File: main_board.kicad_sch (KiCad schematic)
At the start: 15 parts, among them J1 MEGA_SARJ, J2 POWER, J3 I2C, J4 FREE_GPIO, J5 5V, J6 12V, J7 24V, J8 GND, J9 GND, U1 BNO055_IMU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

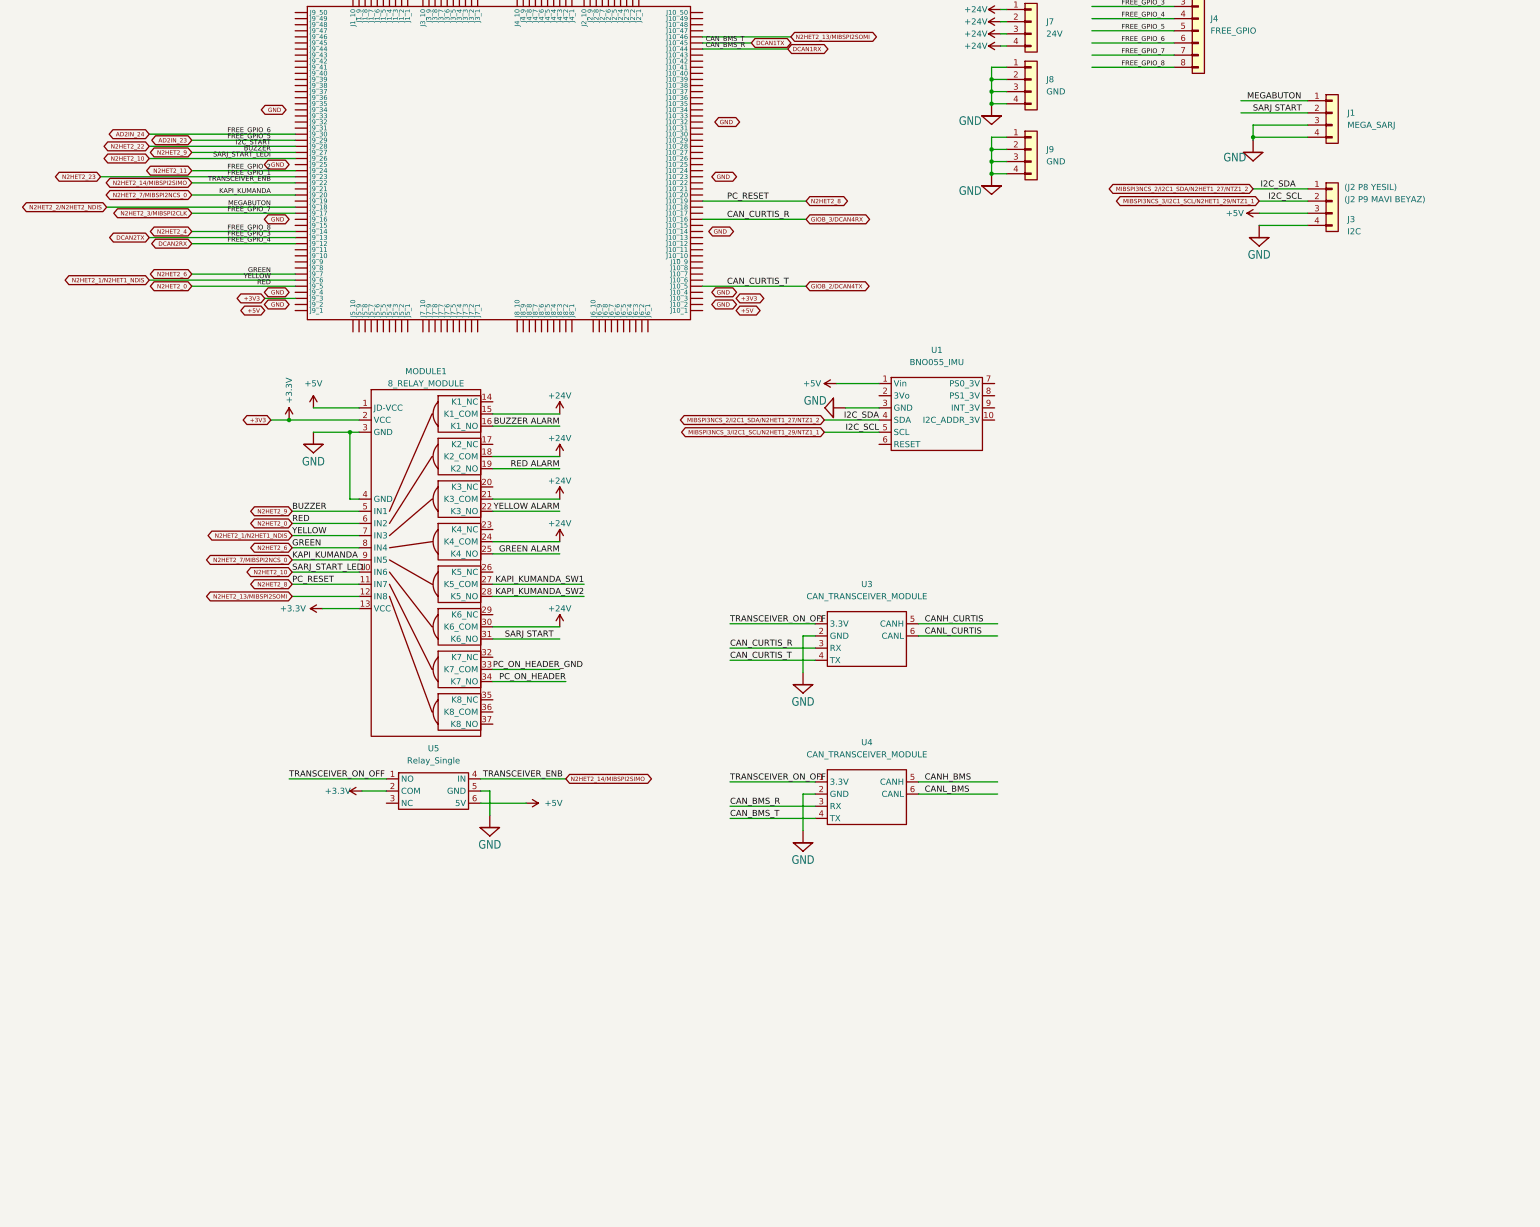
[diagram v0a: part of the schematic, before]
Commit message: Deleting Relays Adding MOSFETs
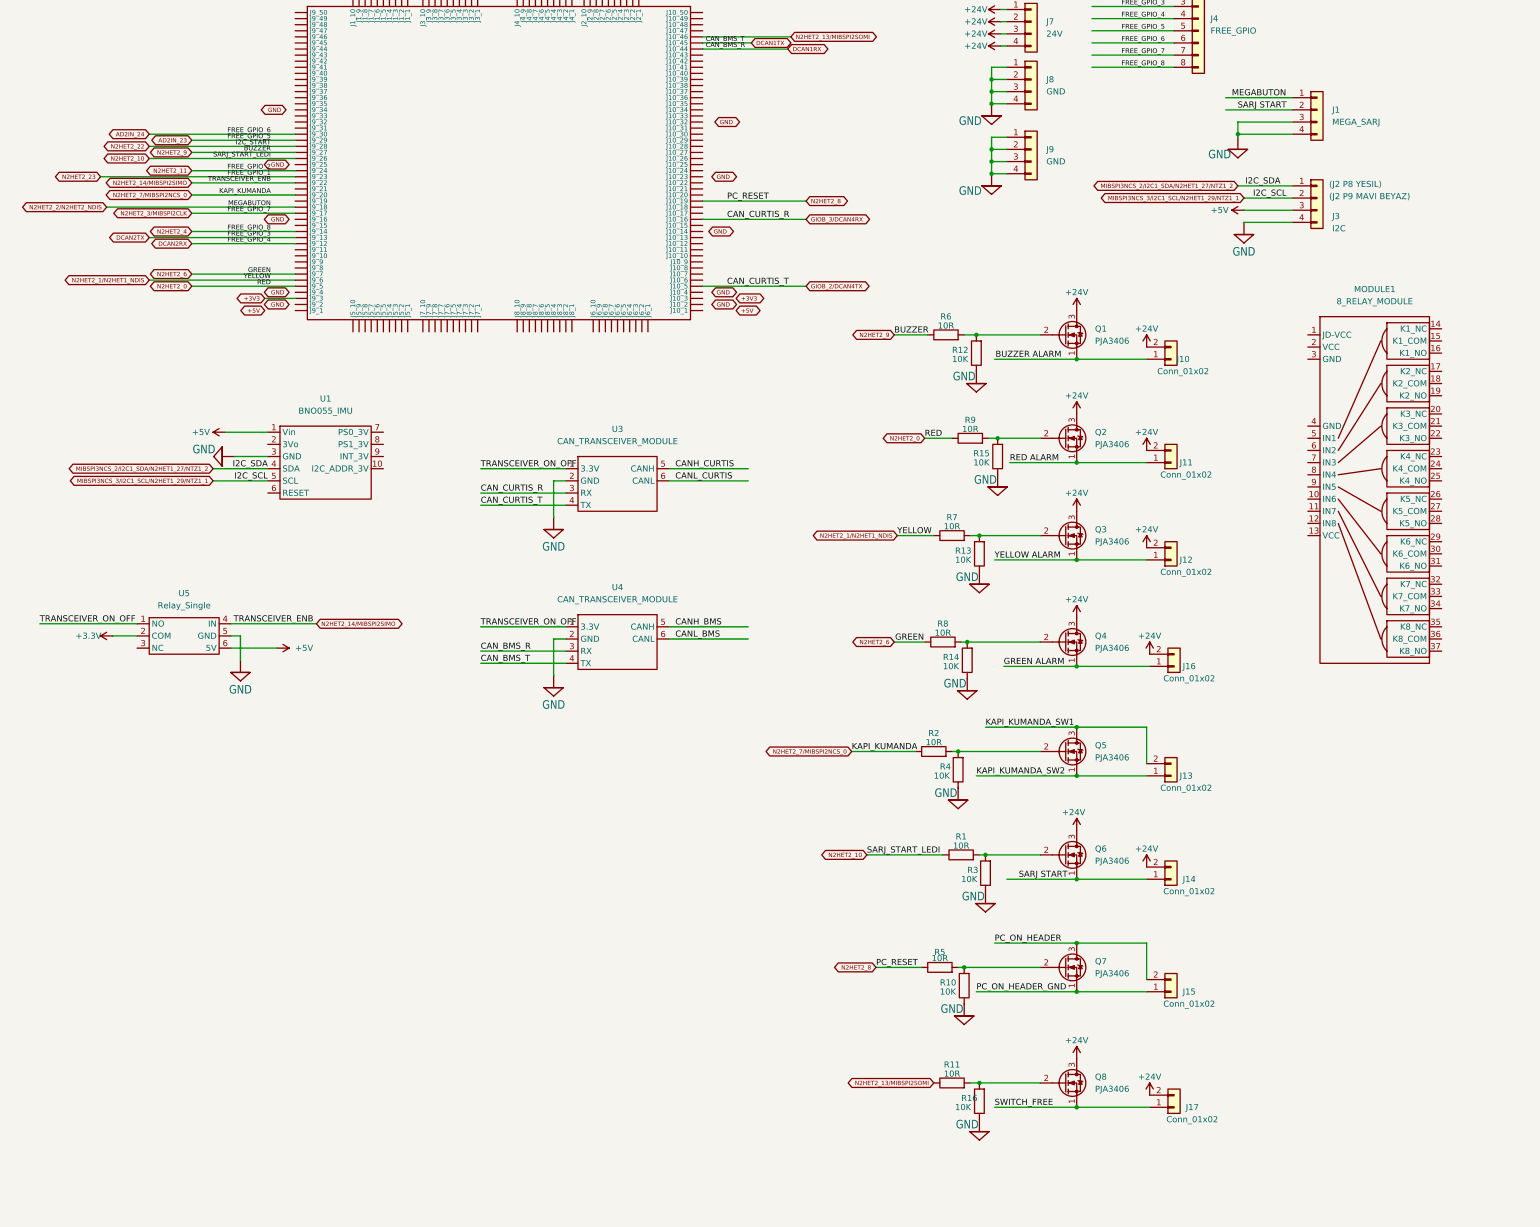
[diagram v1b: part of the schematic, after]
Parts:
- added J10, J11, J12, J13, J14, J15, J16, J17: Conn_01x02, Connector_Phoenix_MC_HighVoltage:PhoenixContact_MCV_1,5_2-G-5.08_1x02_P5.08mm_Vertical, symbol Connector_Generic:Conn_01x02
- added Q1, Q2, Q3, Q4, Q5, Q6, Q7, Q8: PJA3406, Package_TO_SOT_SMD:SOT-23, symbol Transistor_FET:2N7000
- added R1, R11, R2, R5, R6, R7, R8, R9: 10R, Resistor_SMD:R_0805_2012Metric, symbol Device:R
- added R10, R12, R13, R14, R15, R16, R3, R4: 10K, Resistor_SMD:R_0805_2012Metric, symbol Device:R
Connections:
- net +24V: now also J10.2 (Pin_2), J11.2 (Pin_2), J12.2 (Pin_2), J14.2 (Pin_2), J16.2 (Pin_2), J17.2 (Pin_2), Q1.3 (D), Q2.3 (D), Q3.3 (D), Q4.3 (D), Q6.3 (D), Q8.3 (D); no longer MODULE1.15 (K1_COM), MODULE1.18 (K2_COM), MODULE1.21 (K3_COM), MODULE1.24 (K4_COM), MODULE1.30 (K6_COM)
- net +3.3V: no longer MODULE1.13 (VCC), MODULE1.2 (VCC), U2.J9_3
- net +5V: no longer MODULE1.1 (JD-VCC)
- net BUZZER ALARM: now also J10.1 (Pin_1), Q1.1 (S); no longer MODULE1.16 (K1_NO)
- net GND: now also R10.1, R12.1, R13.1, R14.1, R15.1, R16.1, R3.1, R4.1; no longer MODULE1.3 (GND), MODULE1.4 (GND)
- net GREEN ALARM: now also J16.1 (Pin_1), Q4.1 (S); no longer MODULE1.25 (K4_NO)
- net KAPI_KUMANDA_SW1: now also J13.2 (Pin_2), Q5.3 (D); no longer MODULE1.27 (K5_COM)
- net KAPI_KUMANDA_SW2: now also J13.1 (Pin_1), Q5.1 (S); no longer MODULE1.28 (K5_NO)
- net N2HET2_0: now also R9.1; no longer MODULE1.6 (IN2)
- net N2HET2_1/N2HET1_NDIS: now also R7.1; no longer MODULE1.7 (IN3)
- net N2HET2_10: now also R1.1; no longer MODULE1.10 (IN6)
- net N2HET2_13/MIBSPI2SOMI: now also R11.1; no longer MODULE1.12 (IN8)
- net N2HET2_6: now also R8.1; no longer MODULE1.8 (IN4)
- net N2HET2_7/MIBSPI2NCS_0: now also R2.1; no longer MODULE1.9 (IN5)
- net N2HET2_8: now also R5.1; no longer MODULE1.11 (IN7)
- net N2HET2_9: now also R6.1; no longer MODULE1.5 (IN1)
- net PC_ON_HEADER: now also J15.2 (Pin_2), Q7.3 (D); no longer MODULE1.34 (K7_NO)
- net PC_ON_HEADER_GND: now also J15.1 (Pin_1), Q7.1 (S); no longer MODULE1.33 (K7_COM)
- net RED ALARM: now also J11.1 (Pin_1), Q2.1 (S); no longer MODULE1.19 (K2_NO)
- net SARJ START: now also J14.1 (Pin_1), Q6.1 (S); no longer MODULE1.31 (K6_NO)
- net YELLOW ALARM: now also J12.1 (Pin_1), Q3.1 (S); no longer MODULE1.22 (K3_NO)
- new net: Q8.2 (G), R11.2, R16.2
- new net: Q7.2 (G), R10.2, R5.2
- new net: Q2.2 (G), R15.2, R9.2
- new net: Q5.2 (G), R2.2, R4.2
- new net: Q6.2 (G), R1.2, R3.2
- new net: Q1.2 (G), R12.2, R6.2
- new net: Q3.2 (G), R13.2, R7.2
- new net: Q4.2 (G), R14.2, R8.2
- new net +3V3: U2.J9_3
- new net SWITCH_FREE: J17.1 (Pin_1), Q8.1 (S)
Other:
- moved on the sheet: J1, J3, U1, U3, U4, U5
